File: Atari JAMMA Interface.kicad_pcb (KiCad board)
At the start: 2 copper layers, 112.2 x 74.8 mm, 45 parts, among them P1 10K, U1 LM386, U2 DIP-14_W7.62mm_Socket, U3 MC34063AP, U4 74LS04

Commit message: tweaks and cleanup
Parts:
- moved C4 1.64 mm to (161.4, 106.6)
- moved HV/S 0.84 mm to (166.2, 116.0)
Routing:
- net -12V: track 159.0 -> 151.2 mm
- net SPKR+: track 74.8 -> 76.8 mm
- net PREAMP_OUT: track 29.1 -> 27.6 mm
- net VID_SYN1: track 30.5 -> 31.6 mm
- net SWE: track 30.6 -> 29.6 mm
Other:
- board text added: "JP1"
- board text added: "JP5"
- board text added: "SYN 1"
- board text added: "SYN 2"
- board text removed: "SYNC 1"
- board text removed: "SYNC 2"

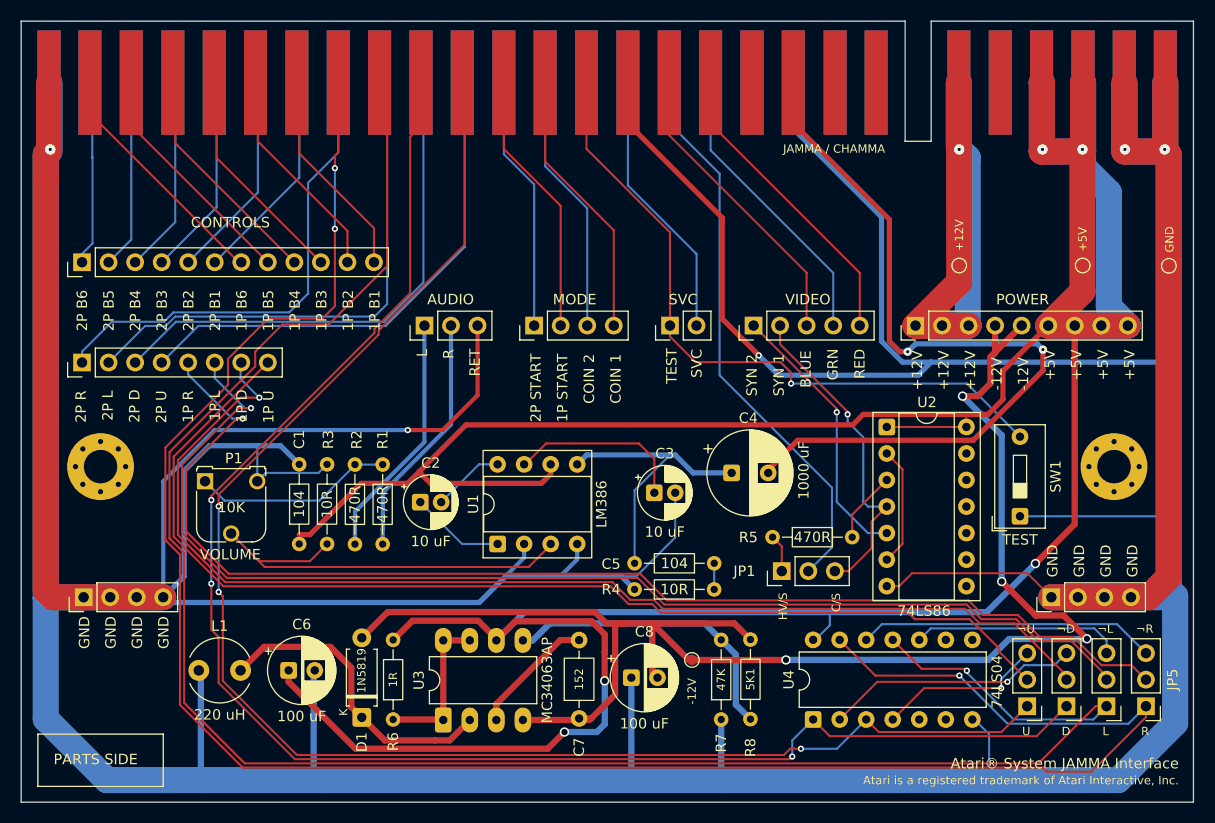
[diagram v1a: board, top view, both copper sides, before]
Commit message: power connections -> 3.96mm
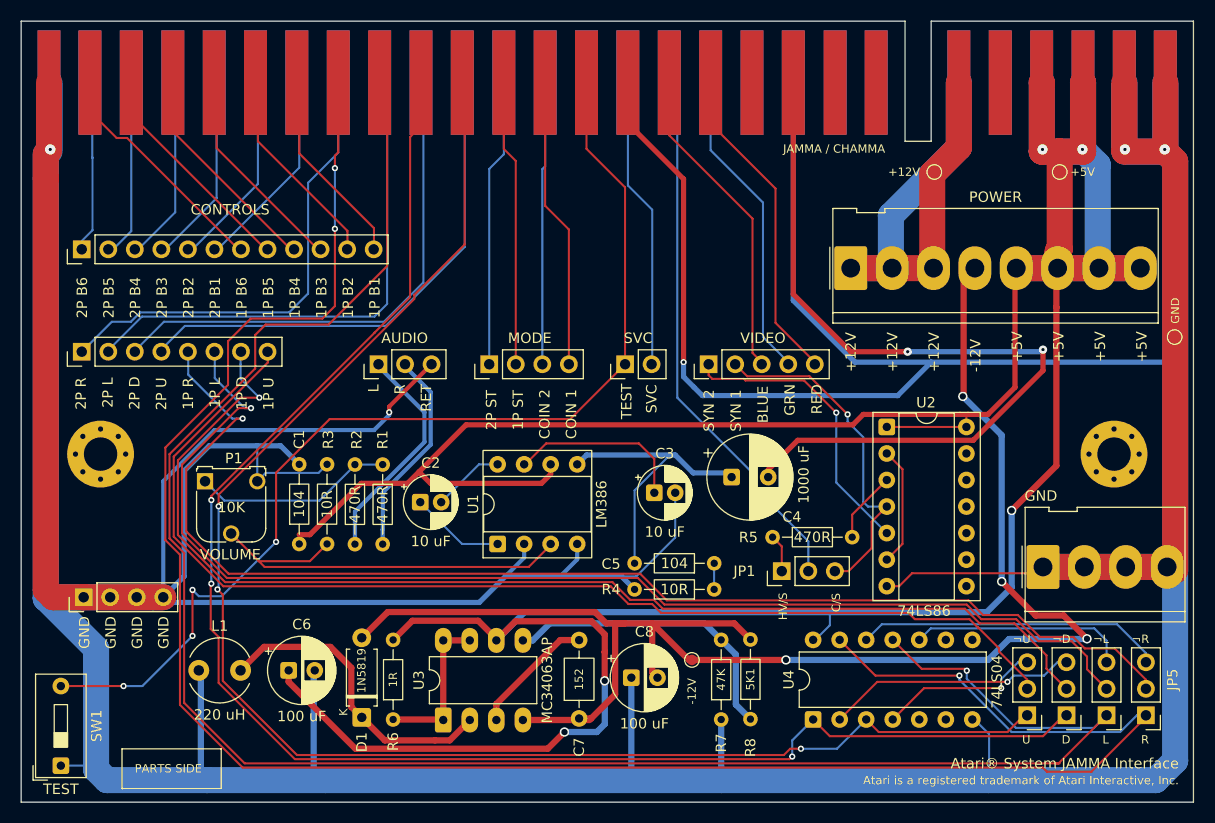
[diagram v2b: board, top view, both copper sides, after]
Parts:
- GND: renamed from Ground; value PinHeader_1x04_P2.54mm_Vertical -> Molex_KK-396_5273-04A_1x04_P3.96mm_Vertical; footprint Connector_PinHeader_2.54mm:PinHeader_1x04_P2.54mm_Vertical -> Connector_Molex:Molex_KK-396_5273-04A_1x04_P3.96mm_Vertical
- POWER: value PinHeader_1x09_P2.54mm_Vertical -> Molex_KK-396_5273-08A_1x08_P3.96mm_Vertical; footprint Connector_PinHeader_2.54mm:PinHeader_1x09_P2.54mm_Vertical -> Connector_Molex:Molex_KK-396_5273-08A_1x08_P3.96mm_Vertical
- moved TEST 94.9 mm to (97.2, 134.6)
- moved +12V 9.26 mm to (180.8, 77.8), turned to 180 degrees
- moved +5V 9.22 mm to (192.8, 77.8), turned to 180 degrees
- moved POWER 8.29 mm to (172.8, 87.0), turned to 0 degrees
- moved GND 6.84 mm to (203.8, 93.6)
- moved AUDIO 5.75 mm to (127.6, 96.2)
- moved MODE 5.67 mm to (138.2, 96.2)
- moved SVC 5.67 mm to (151.2, 96.2)
- moved VIDEO 5.67 mm to (159.2, 96.2)
- moved GND 3.01 mm to (191.2, 115.6), turned to 0 degrees
- moved CONTROLS 1.23 mm to (99.2, 85.2)
- moved REF** 1.20 mm to (101.0, 104.8)
- moved REF** 1.20 mm to (198.0, 104.8)
- moved DIRECTIONALS 1.03 mm to (99.2, 95.0)
- moved HV/S 0.87 mm to (197.3, 129.8)
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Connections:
- POWER pad 5: -12V -> +5V
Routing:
- net TEST: track 65.7 -> 102.2 mm, vias 1 -> 4
- net GND: track 734.2 -> 724.0 mm
- net +12V: track 61.1 -> 51.2 mm, vias 1 -> 0
- net +5V: track 340.2 -> 344.4 mm
- net AUDIO_R: track 23.6 -> 20.1 mm
- net 2P_START: track 24.5 -> 27.5 mm
- net SPKR+: track 76.8 -> 79.5 mm
- net VID_G: track 28.1 -> 30.3 mm
- net VID_R: track 29.2 -> 31.4 mm
- net VID_B: track 28.7 -> 30.9 mm
- net COIN_2: track 24.9 -> 27.1 mm
- net VID_SYN2: track 26.2 -> 28.3 mm
- net SERVICE: track 26.0 -> 27.9 mm
- net 1P_START: track 25.5 -> 27.4 mm
- net 1P_L_OUT: track 116.0 -> 118.0 mm
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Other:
- board text added: "1P ST"
- board text added: "2P ST"
- board text removed: "1P START"
- board text removed: "2P START"

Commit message: minor cleanup
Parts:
- moved Ground 0.98 mm to (98.4, 118.5)
- moved L1 0.80 mm to (109.6, 125.5)
- moved C6 0.80 mm to (118.2, 125.5)
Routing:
- net 1P_B5: track 21.5 -> 23.9 mm
- net GND: track 724.0 -> 724.9 mm
- net 1P_R: track 202.3 -> 203.1 mm
- net 1P_B6: track 22.5 -> 23.4 mm
- net SWE: track 29.6 -> 28.8 mm

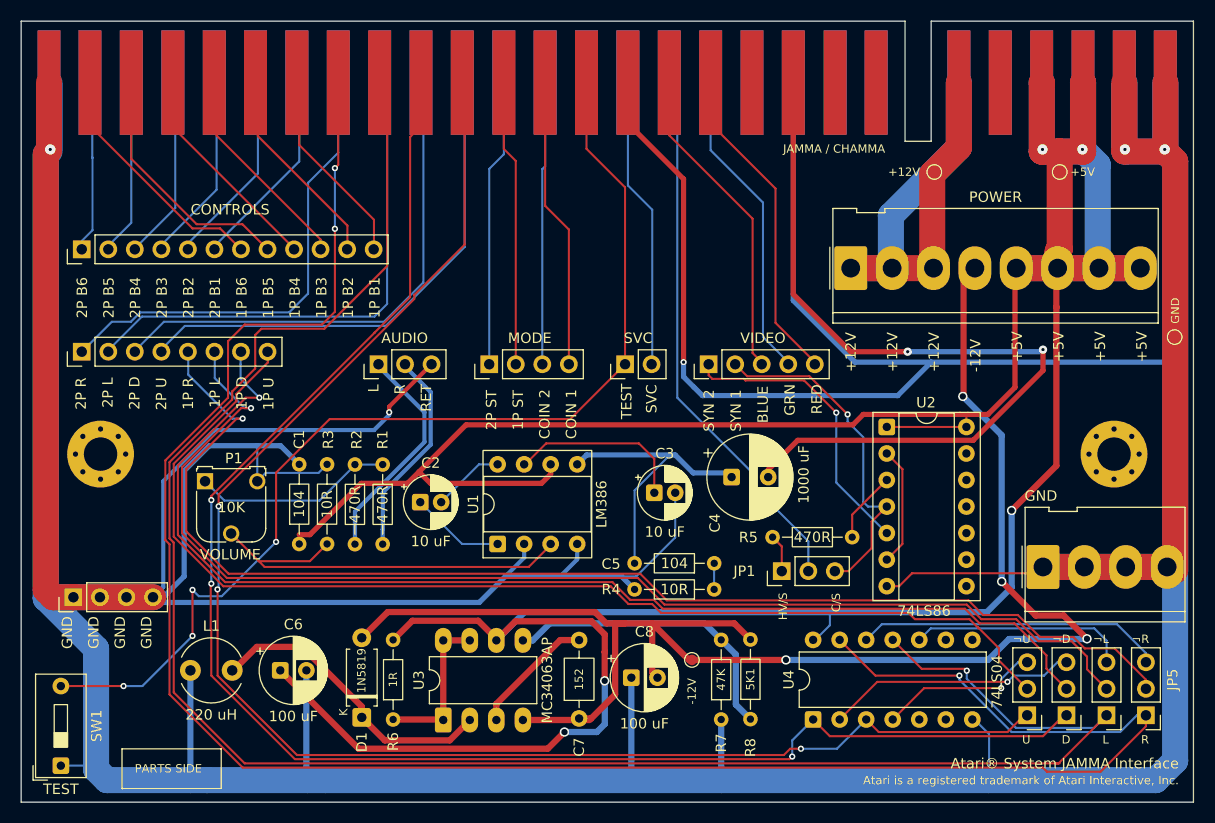
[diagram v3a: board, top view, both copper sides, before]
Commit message: slightly move ground in
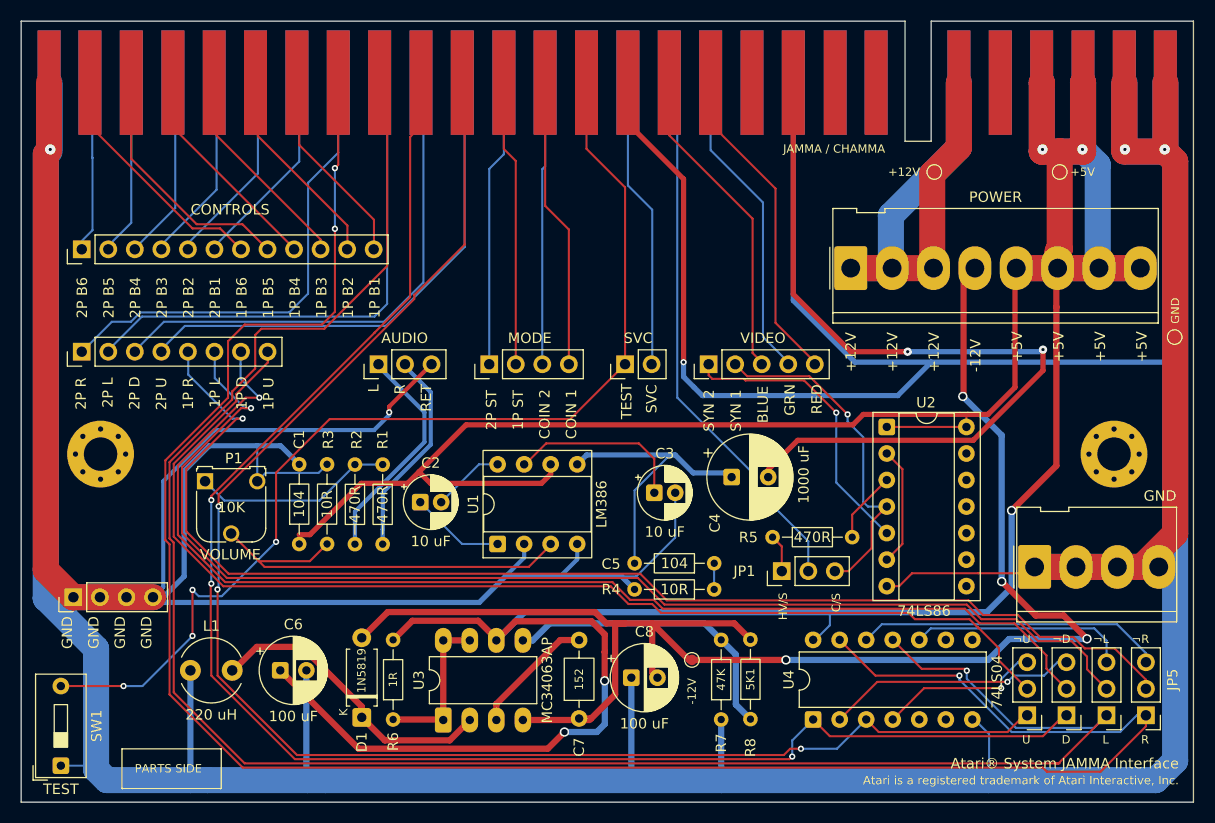
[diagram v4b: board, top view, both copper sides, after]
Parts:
- moved GND 0.80 mm to (190.4, 115.6)
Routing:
- net GND: track 724.9 -> 722.2 mm
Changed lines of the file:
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@@
 	(footprint "Connector_Molex:Molex_KK-396_5273-04A_1x04_P3.96mm_Vertical"
 		(layer "F.Cu")
-		(at 191.2 115.6)
+		(at 190.4 115.6)
 		(descr "Molex KK 396 Interconnect System, old/engineering part number: 5273-04A example for new part number: 09-65-2048, 4 Pins (https://www.molex.com/pdm_docs/sd/009652028_sd.pdf), generated with kicad-footprint-generator")
 		(tags "connector Molex KK-396 vertical")
 		(property "Reference" "GND"
-			(at -0.2 -6.8 0)
+			(at 12 -6.8 0)
 			(layer "F.SilkS" knockout)
 			(effects
@@
 	)
 	(segment
-		(start 151.47 69.2425)
-		(end 151.47 73.1425)
-		(width 0.5)
-		(layer "F.Cu")
-		(net 1)
-	)
-	(segment
-		(start 185 116.2)
-		(end 185.00287 116.20287)
+		(start 176.25 117.44)
+		(end 177.435 117.44)
 		(width 0.2)
 		(layer "F.Cu")
@@
 	)
 	(segment
-		(start 96.45301 118.5)
-		(end 95.75301 117.8)
-		(width 2.5)
-		(layer "F.Cu")
-		(net 1)
-	)
-	(segment
-		(start 178.675 116.2)
-		(end 185 116.2)
-		(width 0.2)
+		(start 151.47 69.2425)
+		(end 151.47 73.1425)
+		(width 0.5)
 		(layer "F.Cu")
 		(net 1)
 	)
 	(segment
-		(start 176.25 117.44)
-		(end 177.435 117.44)
-		(width 0.2)
+		(start 203.849001 112.4)
+		(end 200.649001 115.6)
+		(width 2.5)
 		(layer "F.Cu")
 		(net 1)
@@
 	)
 	(segment
-		(start 98.4 118.5)
-		(end 96.45301 118.5)
-		(width 2.5)
+		(start 189.79713 116.20287)
+		(end 190.4 115.6)
+		(width 0.2)
 		(layer "F.Cu")
 		(net 1)
@@
 	)
 	(segment
-		(start 203.849001 115.950999)
+		(start 203.849001 112.4)
 		(end 203.849003 76.777677)
 		(width 2.5)
@@
 	)
 	(segment
+		(start 200.649001 115.6)
+		(end 190.4 115.6)
+		(width 2.5)
+		(layer "F.Cu")
+		(net 1)
+	)
+	(segment
 		(start 156.8 78.4725)
 		(end 156.8 96)
@@
 	)
 	(segment
-		(start 185.00287 116.20287)
-		(end 190.79713 116.20287)
-		(width 0.2)
+		(start 98.35301 118.5)
+		(end 95.75301 115.9)
+		(width 2.5)
 		(layer "F.Cu")
 		(net 1)
@@
 	)
 	(segment
-		(start 95.75301 117.8)
-		(end 95.75301 76.070195)
+		(start 98.4 118.5)
+		(end 98.35301 118.5)
 		(width 2.5)
 		(layer "F.Cu")
@@
 	)
 	(segment
-		(start 198.98 75.818851)
-		(end 199.001271 75.840122)
+		(start 185.00287 116.20287)
+		(end 189.79713 116.20287)
 		(width 0.2)
 		(layer "F.Cu")
@@
 	)
 	(segment
-		(start 190.79713 116.20287)
-		(end 191.2 115.8)
+		(start 198.98 75.818851)
+		(end 199.001271 75.840122)
 		(width 0.2)
 		(layer "F.Cu")
@@
 	)
 	(segment
-		(start 96.07 75.797186)
-		(end 96.112936 75.840122)
+		(start 185 116.2)
+		(end 185.00287 116.20287)
 		(width 0.2)
 		(layer "F.Cu")
@@
 	)
 	(segment
-		(start 191.2 115.8)
-		(end 191.2 115.6)
+		(start 95.75301 115.9)
+		(end 95.75301 76.070195)
+		(width 2.5)
+		(layer "F.Cu")
+		(net 1)
+	)
+	(segment
+		(start 96.07 75.797186)
+		(end 96.112936 75.840122)
 		(width 0.2)
 		(layer "F.Cu")
@@
 	)
 	(segment
-		(start 191.2 115.6)
-		(end 203.08 115.6)
-		(width 2.5)
+		(start 178.675 116.2)
+		(end 185 116.2)
+		(width 0.2)
 		(layer "F.Cu")
 		(net 1)
@@
 	)
 	(segment
-		(start 203.08 115.6)
-		(end 191.2 115.6)
+		(start 202.28 115.6)
+		(end 190.4 115.6)
 		(width 2.5)
 		(layer "B.Cu")
